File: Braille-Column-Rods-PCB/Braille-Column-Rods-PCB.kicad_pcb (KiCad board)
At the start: 2 copper layers, 95 x 99 mm, 154 parts, among them J1 Conn_01x03, J3 Conn_01x02, J4 Conn_01x08, J5 Screw_Terminal_01x02, J6 Screw_Terminal_01x02, J7 Conn_01x02, M1 Stepper_Motor_bipolar, M10 Motor_DC_With_MP, M11 Motor_DC_With_MP, M12 Motor_DC_With_MP, M2 Stepper_Motor_bipolar, M3 Stepper_Motor_bipolar, M4 Stepper_Motor_bipolar, M5 Stepper_Motor_bipolar, M6 Stepper_Motor_bipolar, M7 Stepper_Motor_bipolar, M8 Stepper_Motor_bipolar, M9 Motor_DC_With_MP, SW1 Tactile Button, 160gf, SW2 Tactile Button, 160gf, U1 DRV8847SPWR, U10 AD116, U11 AD116, U12 AD116, U13 AD116, U14 74HC595, U15 74HC595, U17 MT9101ET, U18 MT9101ET, U19 MT9101ET, U2 DRV8847SPWR, U20 MT9101ET, U21 MT9101ET, U22 MT9101ET, U23 MT9101ET, U24 MT9101ET, U25 MT9101ET, U26 MT9101ET, U27 MT9101ET, U28 MT9101ET, U3 RP2040-Zero, U30 CD74HC4067M, U4 DRV8847SPWR, U5 DRV8847SPWR, U6 DRV8847SPWR, U7 DRV8847SPWR, U8 DRV8847SPWR, U9 DRV8847SPWR

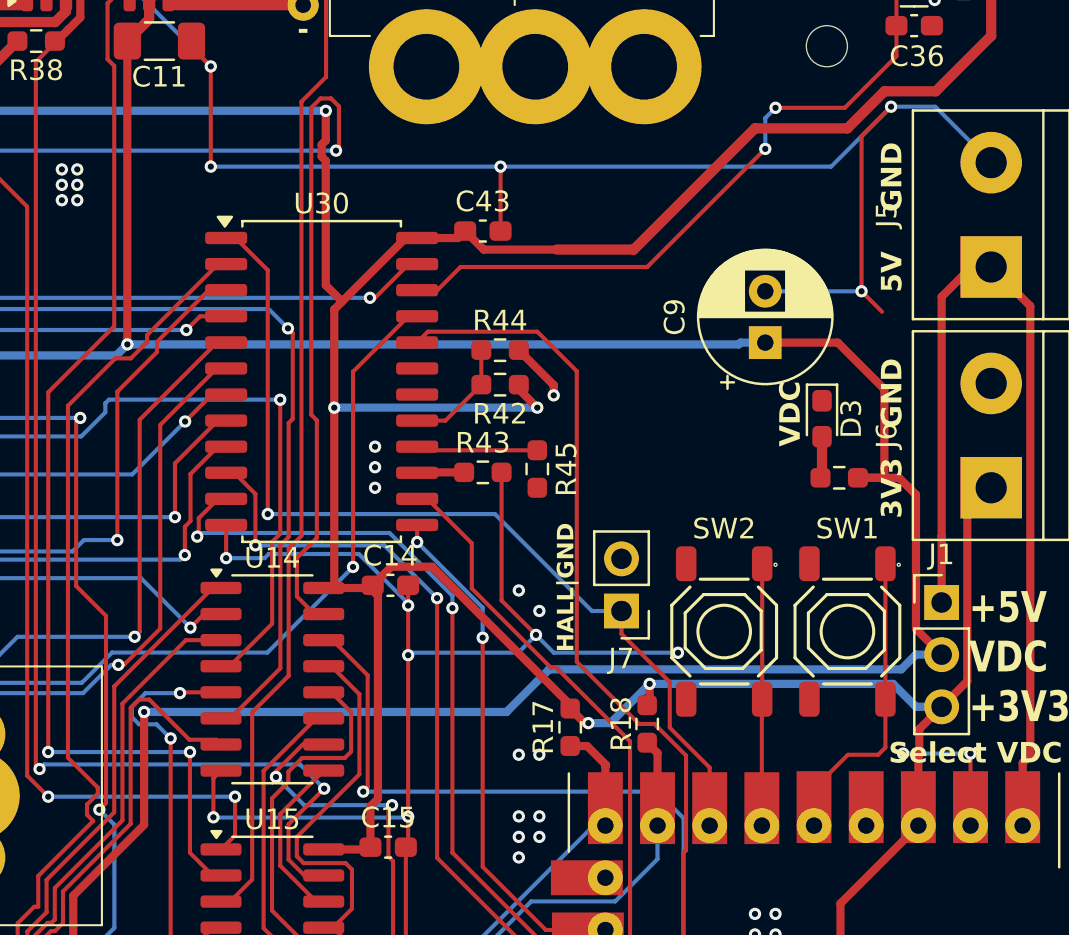
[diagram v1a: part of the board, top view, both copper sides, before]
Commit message: feat: add INA219 current sensor
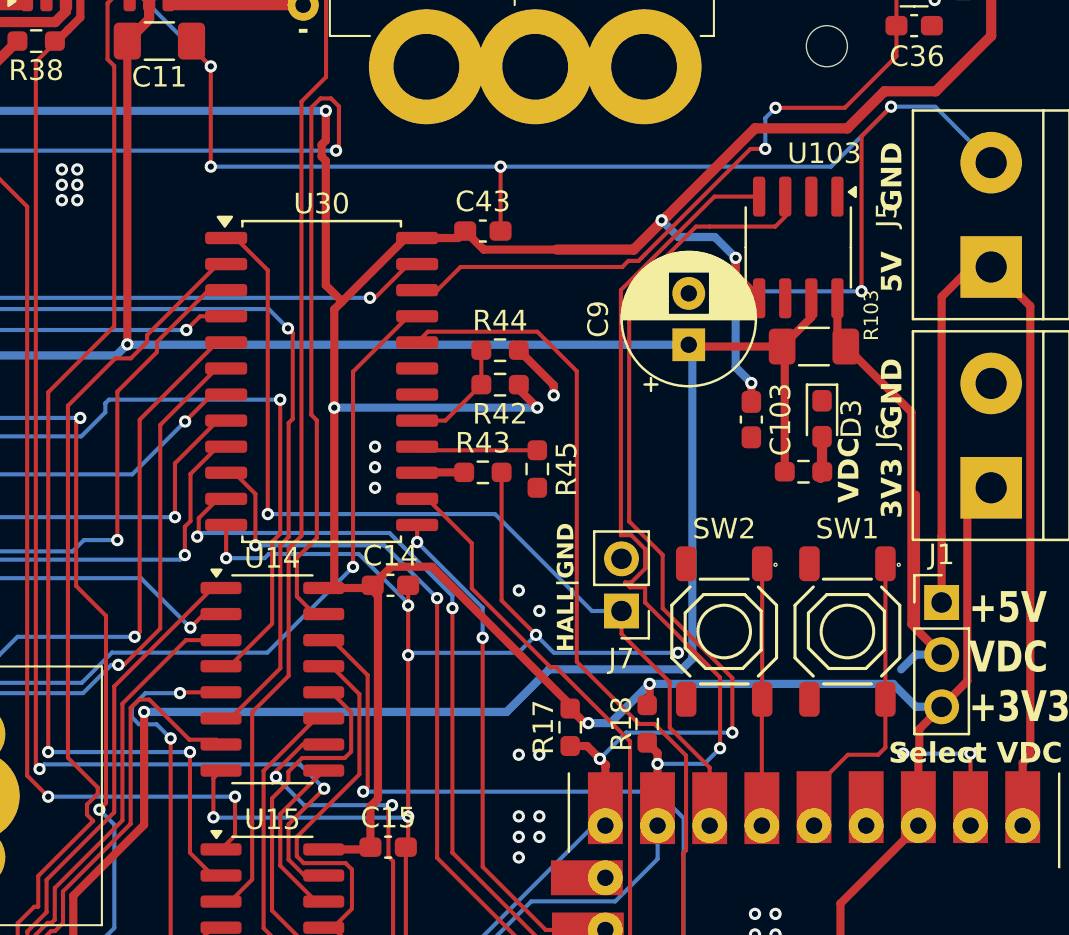
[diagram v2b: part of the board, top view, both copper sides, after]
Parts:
- added C103: 100n, Capacitor_SMD:C_0603_1608Metric_Pad1.08x0.95mm_HandSolder, F.Cu at (163.3, 106.7)
- added R103: 0.1R, Resistor_SMD:R_1206_3216Metric_Pad1.30x1.75mm_HandSolder, F.Cu at (166.4, 103.1)
- added U103: INA219AxD, Package_SO:SOIC-8_3.9x4.9mm_P1.27mm, F.Cu at (165.6, 98.3)
- D1, D10, D11, D5, D6, D7, D8, D9: value LED -> RED_LED
- U10, U11, U12, U13: value AD116 -> AD116_or_BDR6120S
- moved C9 3.73 mm to (160.3, 103.0)
- moved R3 1.76 mm to (165.9, 109.2), turned to 0 degrees
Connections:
- J1 pad 2: VDC -> Net-(J1-Pin_2)
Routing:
- net I2C_SDA: track 153.4 -> 194.0 mm, vias 10 -> 12
- net I2C_SCL: track 157.5 -> 195.5 mm, vias 8 -> 10
- net Net-(J1-Pin_2): track 0.00 -> 30.0 mm
- net +3V3: track 454.7 -> 469.2 mm, vias 14 -> 17
- net VDC: track 294.3 -> 283.6 mm
- net GND: track 322.4 -> 321.0 mm

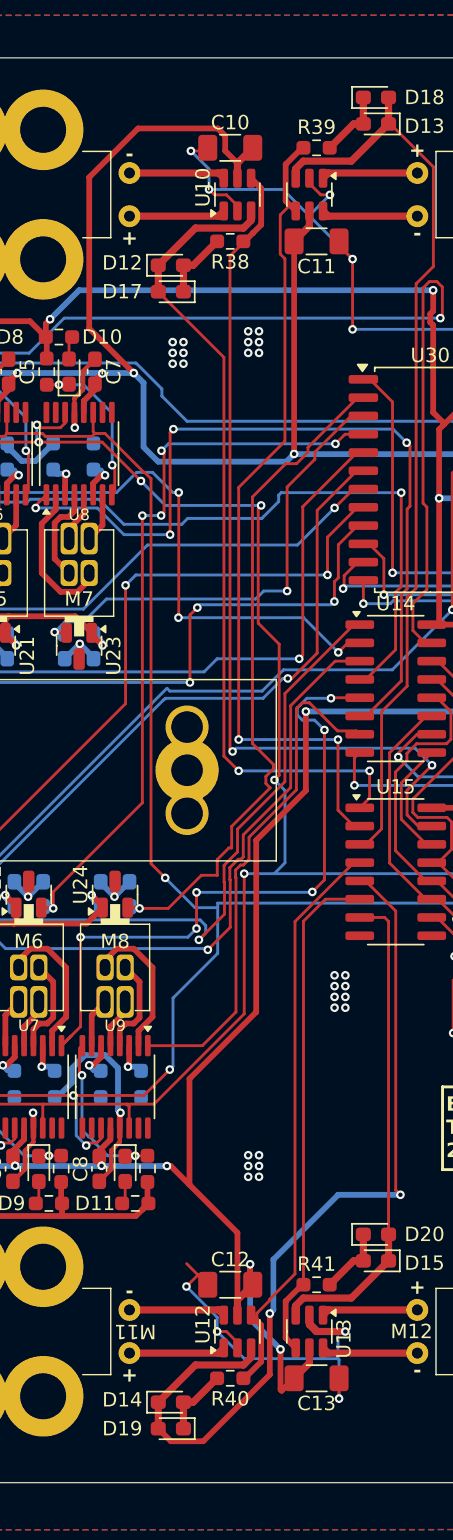
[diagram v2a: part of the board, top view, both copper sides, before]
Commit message: fix(pcb,layout): move capacitors farther from DC motor drivers
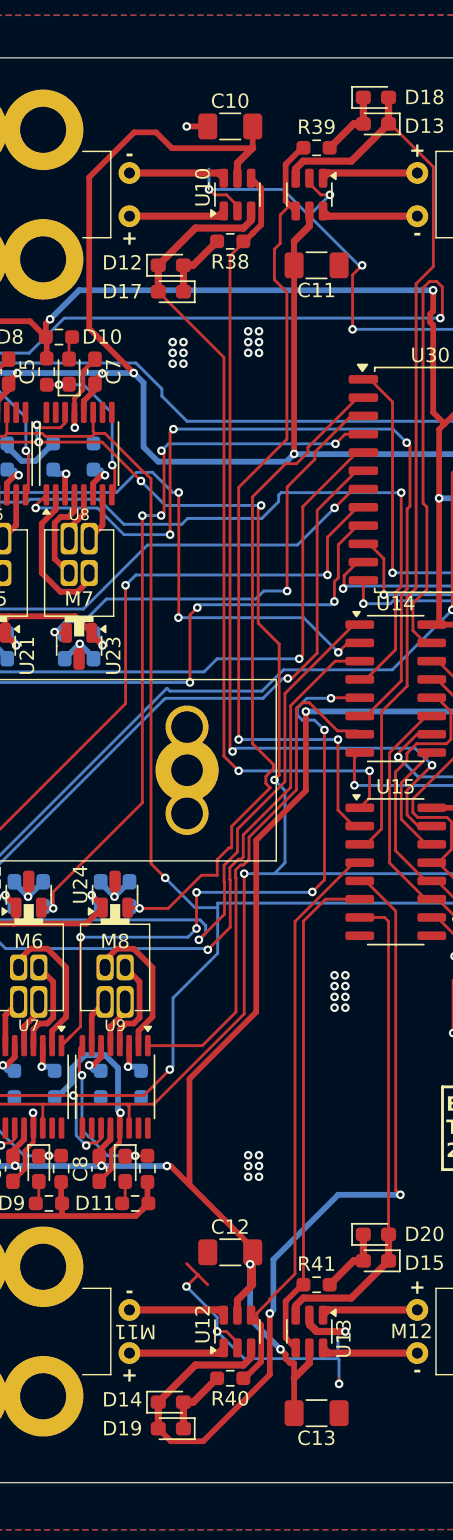
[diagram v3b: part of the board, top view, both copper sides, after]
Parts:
- moved C13 2.42 mm to (134.5, 169.7)
- moved C12 2.25 mm to (128.5, 158.5)
- moved C11 1.67 mm to (134.5, 89.9)
- moved C10 1.49 mm to (128.5, 80.3)
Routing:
- net VDC: track 283.6 -> 289.0 mm
- net GND: track 321.0 -> 316.7 mm

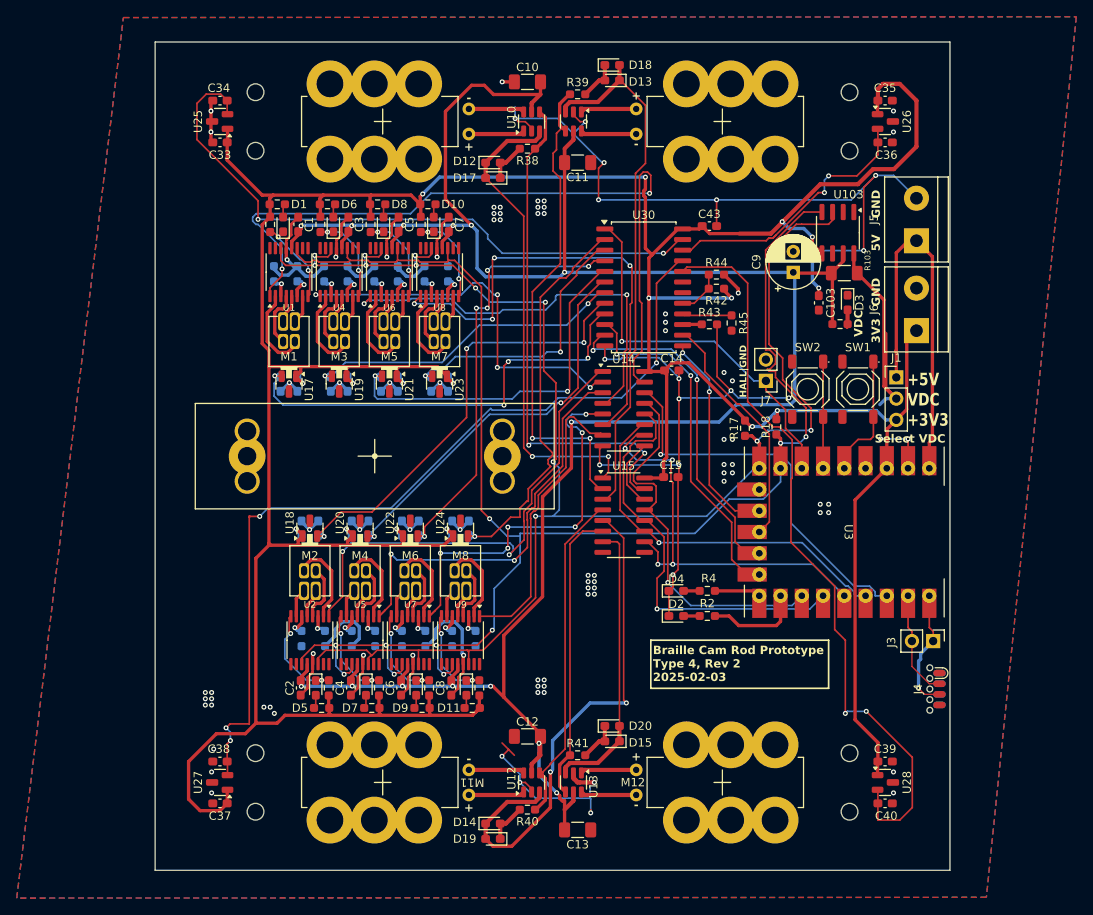
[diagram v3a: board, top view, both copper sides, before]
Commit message: Bump version, update motor footprint precision
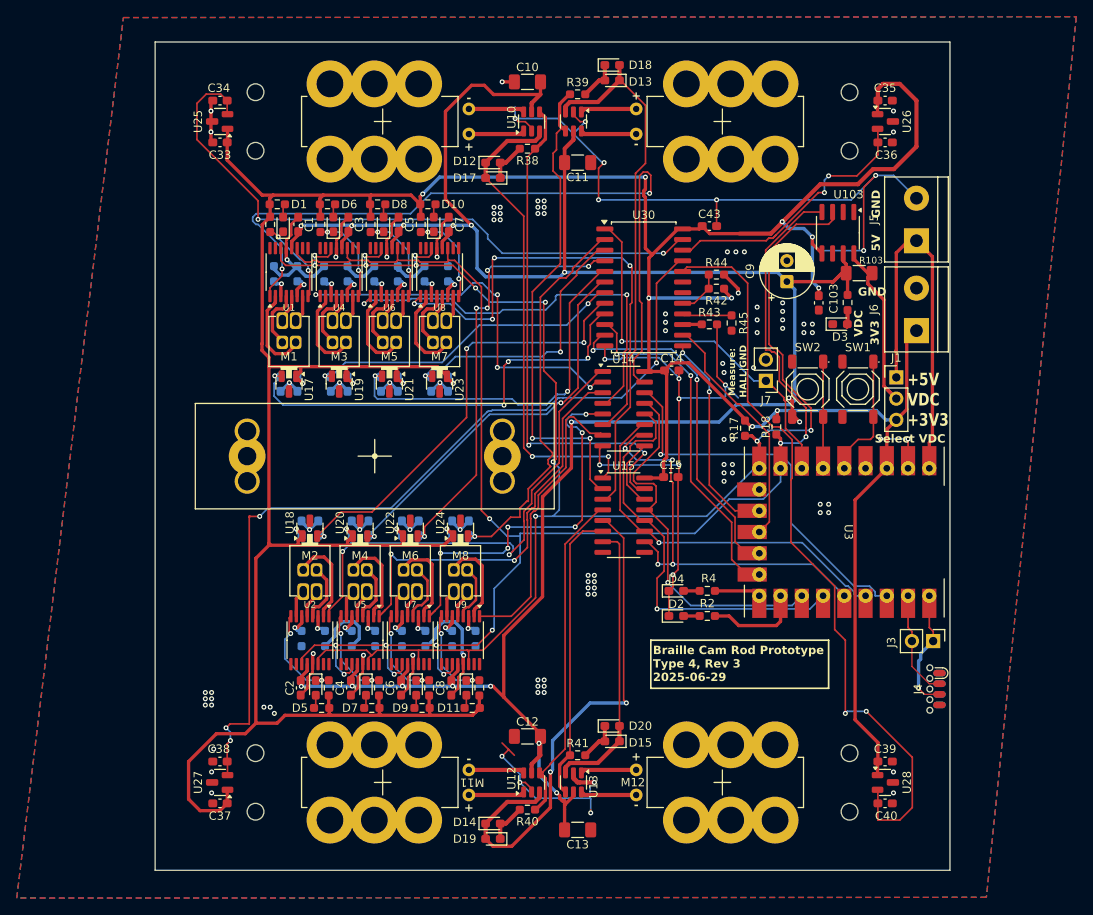
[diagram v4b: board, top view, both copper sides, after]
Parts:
- moved D3 2.73 mm to (165.9, 109.2), turned to 0 degrees
- moved R3 2.73 mm to (166.8, 106.6), turned to -90 degrees
- moved R103 1.78 mm to (168.1, 103.1)
- moved C9 1.34 mm to (159.5, 104.1)
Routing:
- net Net-(J1-Pin_2): track 30.0 -> 21.9 mm
- net GND: track 316.7 -> 314.6 mm, vias 99 -> 115
- net I2C_SCL: track 195.5 -> 194.2 mm
- net Net-(U5-OUT1): track 10.5 -> 11.4 mm
- net VDC: track 289.0 -> 288.1 mm
- net Net-(U2-OUT1): track 10.5 -> 11.2 mm
- net /Motor_Control/HALL_4: track 44.1 -> 44.7 mm
- net Net-(U7-OUT1): track 10.5 -> 11.1 mm
- net Net-(U9-OUT1): track 10.5 -> 11.0 mm
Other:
- board text added: "3V3"
- board text added: "Braille Cam Rod Prototype Type 4, Rev 3 2025-06-29"
- board text added: "GND"
- board text added: "Measure:"
- board text removed: "3V3 GND"
- board text removed: "Braille Cam Rod Prototype Type 4, Rev 2 2025-02-03"

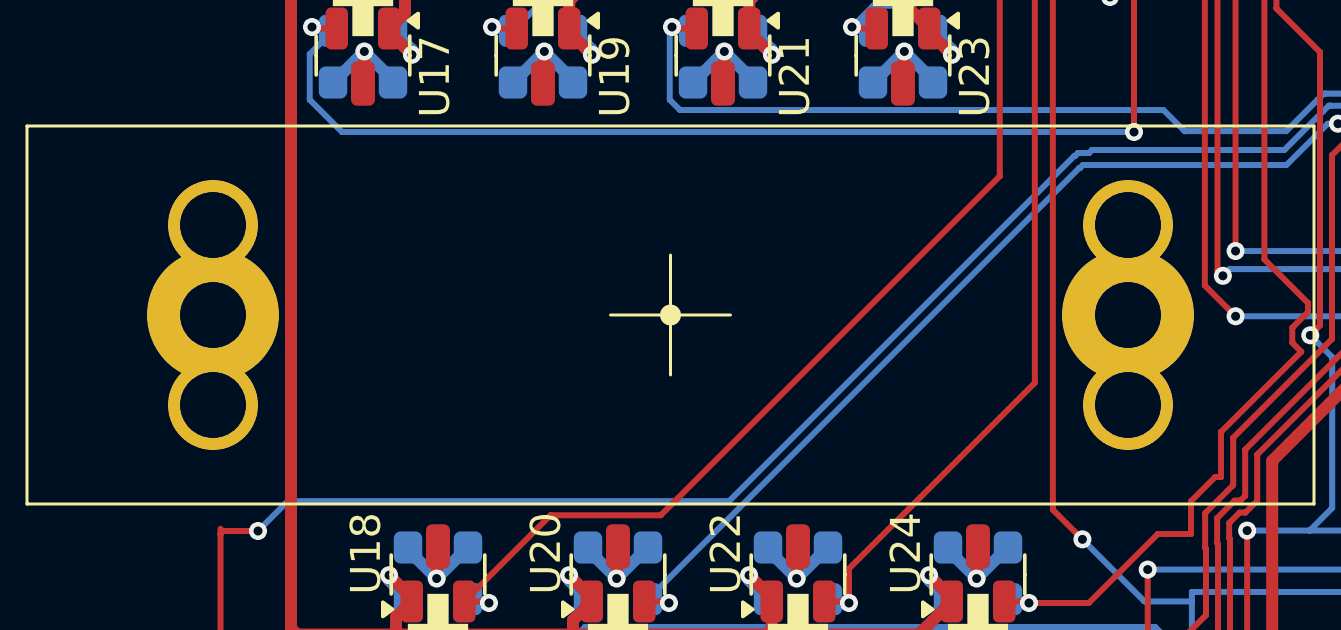
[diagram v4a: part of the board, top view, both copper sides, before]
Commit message: Shink housing mounting holes from 2.2mm to 2.0mm
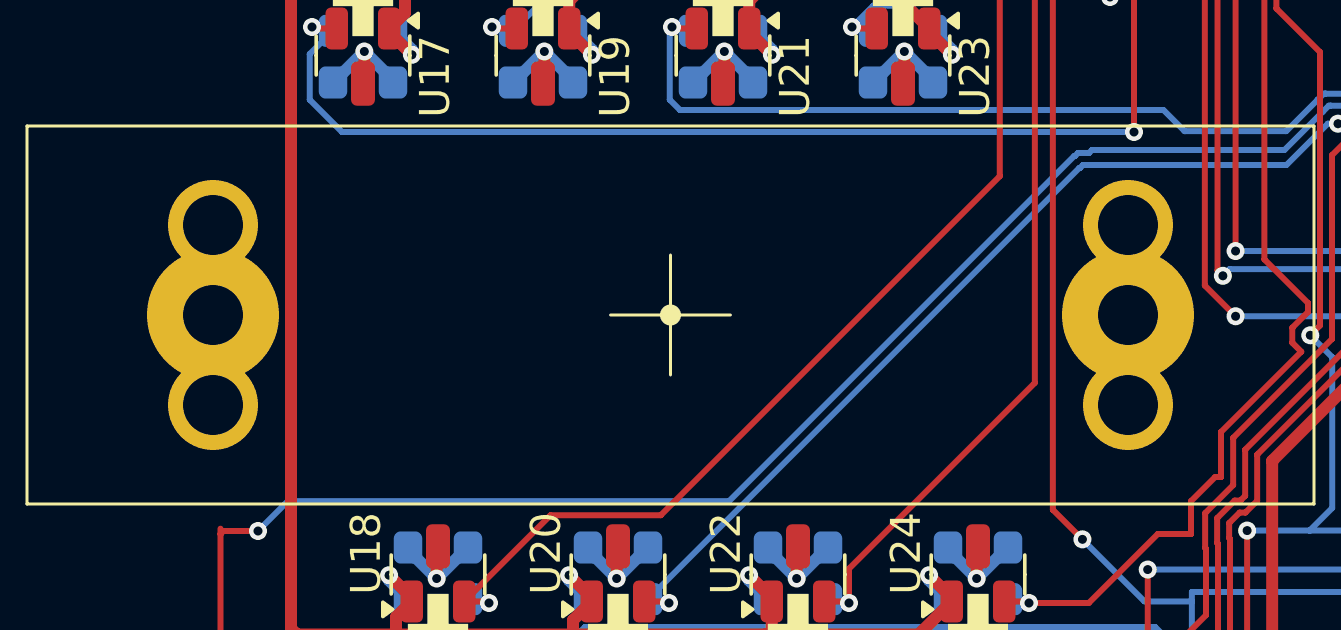
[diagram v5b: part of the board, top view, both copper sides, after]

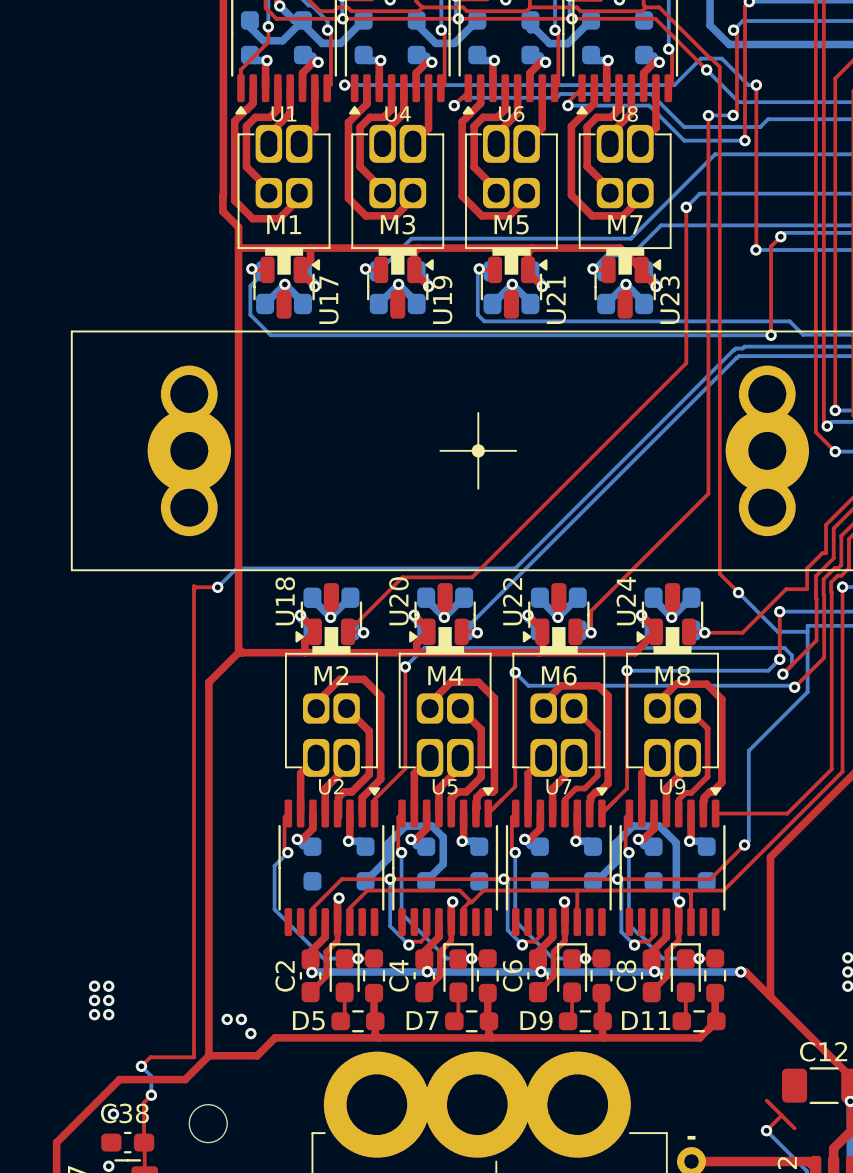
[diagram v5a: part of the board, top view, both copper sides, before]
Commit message: Add PTHs under dots for each cell
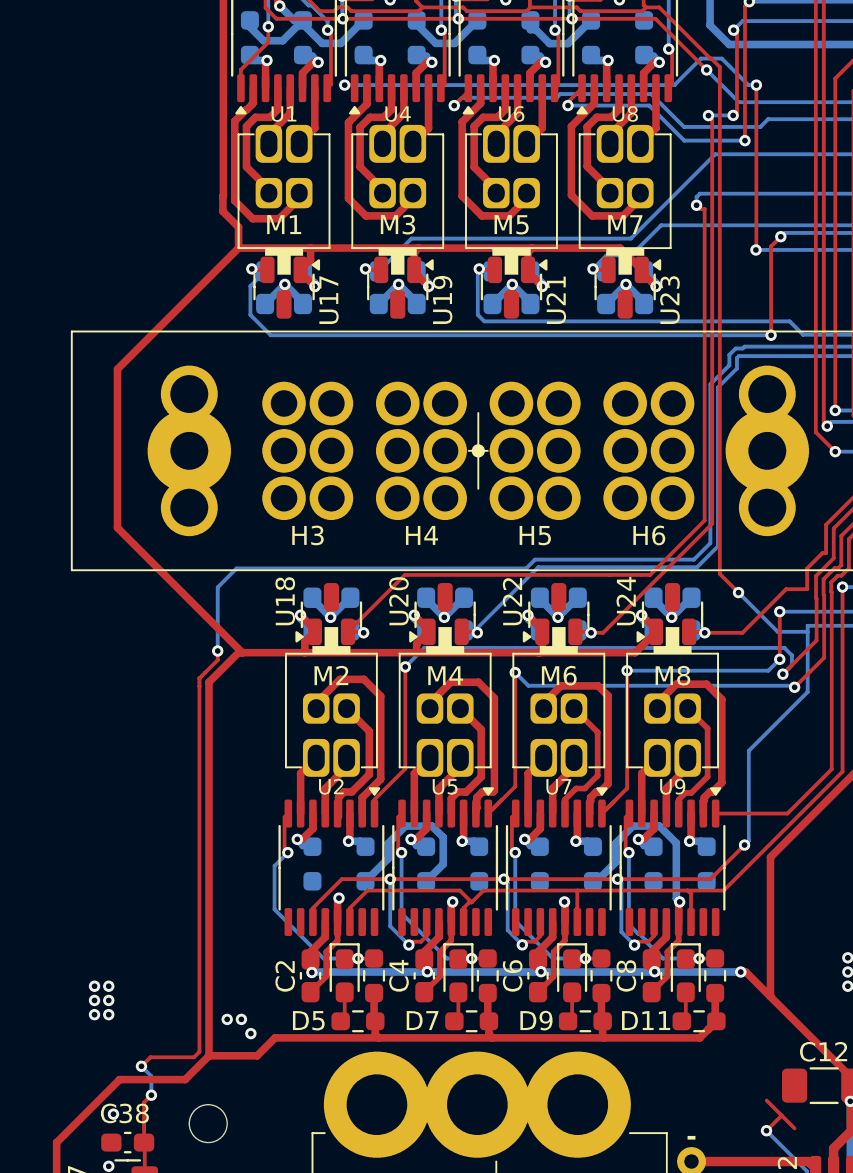
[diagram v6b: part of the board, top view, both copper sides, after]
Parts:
- added H3: BrailleCell, 00-lib-footprints:BrailleCell, F.Cu at (101.2, 125.0)
- added H4: BrailleCell, 00-lib-footprints:BrailleCell, F.Cu at (107.2, 125.0)
- added H5: BrailleCell, 00-lib-footprints:BrailleCell, F.Cu at (113.2, 125.0)
- added H6: BrailleCell, 00-lib-footprints:BrailleCell, F.Cu at (119.2, 125.0)
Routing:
- net /Motor_Control/HALL_1: track 53.8 -> 59.8 mm
- net +3V3: track 469.2 -> 474.5 mm
- net /Motor_Control/HALL_3: track 48.2 -> 53.4 mm
- net /Motor_Control/HALL_10: track 104.0 -> 108.3 mm
- net /Motor_Control/HALL_5: track 51.9 -> 52.5 mm
